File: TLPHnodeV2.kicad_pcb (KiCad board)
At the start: 4 copper layers, 28 x 20.5 mm, 34 parts, among them P3 USB (power only), SW1 Reset, U1 NCP703, U2 LD39130S, U3 LPS25HB, U4 Si7006-A20, U5 ESP-12E, U6 ISL29035, U7 bq25070

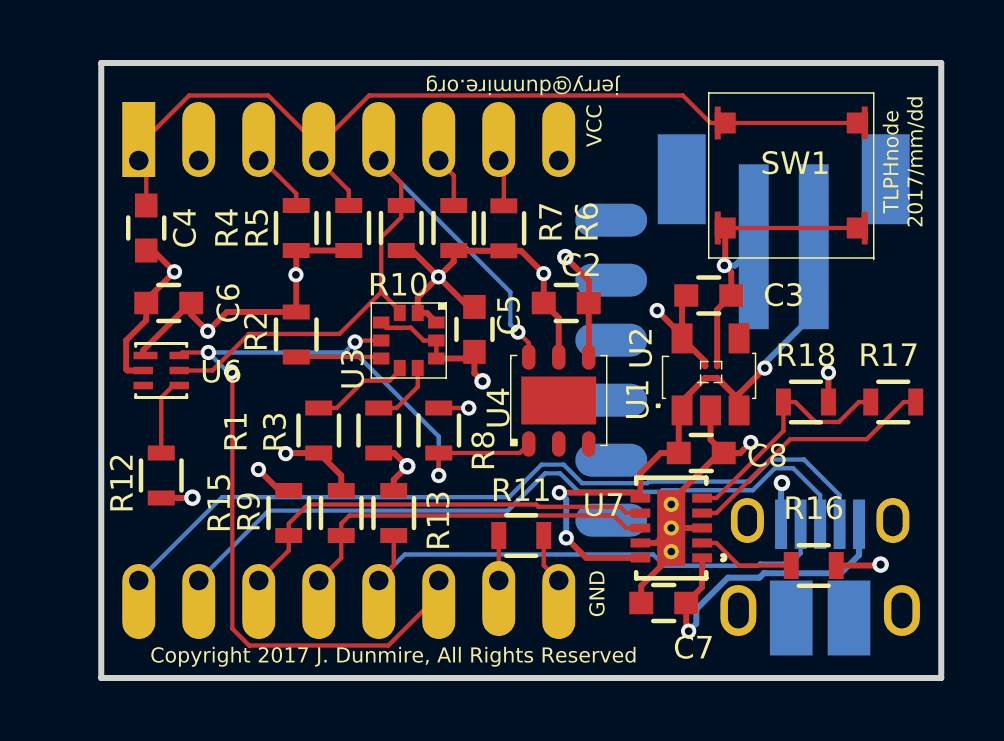
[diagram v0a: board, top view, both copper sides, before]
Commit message: Move traces and add logo
    - move a few traces so that they won't be exposed through the solder
      mask
    - Add a logo
    - Set the date

On branch master
modified:   TLPHnodeV2.kicad_pcb
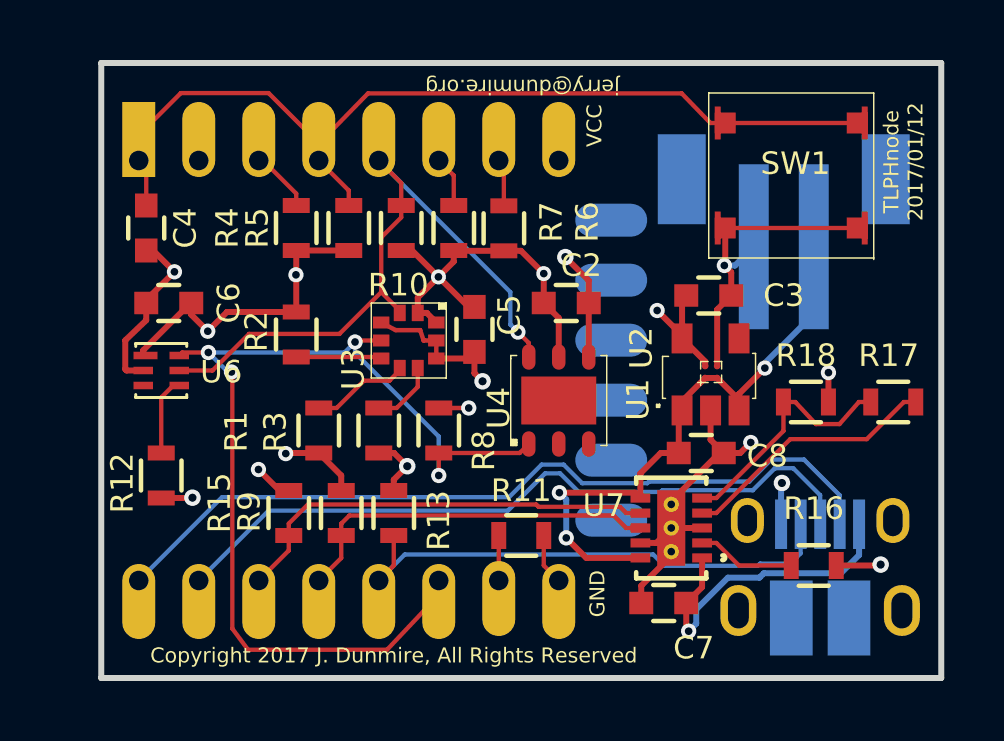
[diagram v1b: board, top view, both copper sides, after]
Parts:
- added Ref**: RockingDLogo_9x7, rockingDLogos:RockingDLogo_9x7, B.Cu at (143.0, 90.9)
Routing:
- net Net-(C4-Pad1): track 30.9 -> 31.5 mm
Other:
- board text added: "TLPHnode 2017/01/12"
- board text removed: "TLPHnode 2017/mm/dd"
